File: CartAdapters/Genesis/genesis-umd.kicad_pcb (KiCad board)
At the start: 2 copper layers, 26.7 x 94.6 mm, 6 parts, among them CON101 UMDv2-CONN, CON102 GENESIS-CONN, U101 MCP23008T-E_SS

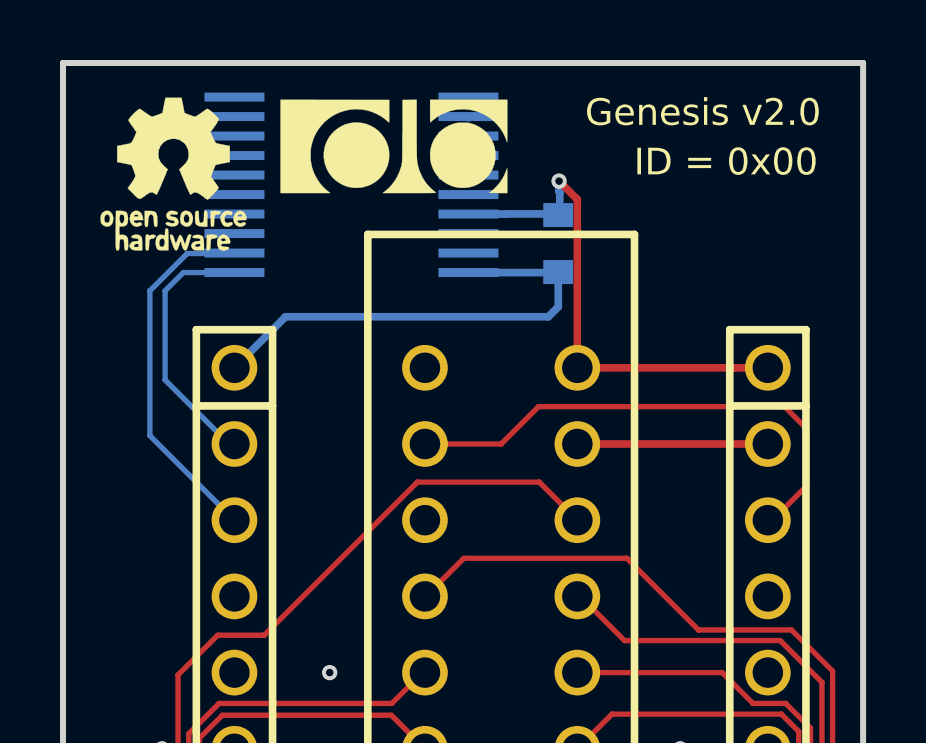
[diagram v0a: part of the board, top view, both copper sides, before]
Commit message: added 0 jumpers for nWR pin selection to support legacy Bitmap Bureau PCBs
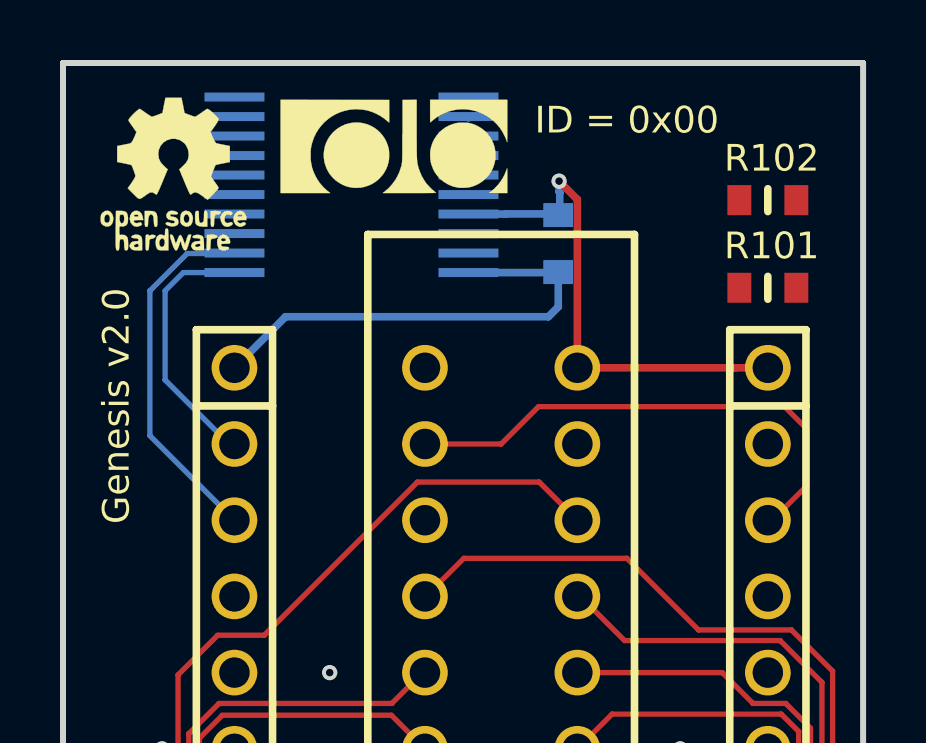
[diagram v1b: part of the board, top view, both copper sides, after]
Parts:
- added R101: 0, db-smt:0603, F.Cu at (153.7, 63.4)
- added R102: 0, db-smt:0603, F.Cu at (153.7, 60.5)
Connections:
- CON102 pad A2: /5V_0 -> Net-(CON102-PadA2)
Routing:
- net /5V_0: track 6.38 -> 0.00 mm
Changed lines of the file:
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@@
     (thickness 1.6)
     (drawings 7)
-    (tracks 500)
+    (tracks 499)
     (zones 0)
-    (modules 6)
-    (nets 58)
+    (modules 8)
+    (nets 59)
   )
   (page A4)
@@
   (net 56 /5V_0)
   (net 57 /5V_1)
+  (net 58 "Net-(CON102-PadA2)")
   (net_class Default "This is the default net class."
     (clearance 0.1778)
@@
     (uvia_dia 0.3)
     (uvia_drill 0.1)
+    (add_net /A0)
     (add_net /A1)
     (add_net /A10)
@@
     (add_net /~VRES~)
     (add_net /~WR~)
+    (add_net "Net-(CON101-Pad25)")
+    (add_net "Net-(CON101-Pad4)")
+    (add_net "Net-(CON101-Pad40)")
+    (add_net "Net-(CON101-Pad5)")
+    (add_net "Net-(CON101-Pad60)")
+    (add_net "Net-(CON101-Pad61)")
+    (add_net "Net-(CON101-Pad65)")
+    (add_net "Net-(CON101-Pad66)")
+    (add_net "Net-(CON102-PadA2)")
+    (add_net "Net-(CON102-PadB1)")
+    (add_net "Net-(CON102-PadB12)")
+    (add_net "Net-(CON102-PadB13)")
+    (add_net "Net-(CON102-PadB14)")
+    (add_net "Net-(CON102-PadB15)")
+    (add_net "Net-(CON102-PadB19)")
+    (add_net "Net-(CON102-PadB21)")
+    (add_net "Net-(CON102-PadB3)")
+    (add_net "Net-(U101-Pad10)")
+    (add_net "Net-(U101-Pad11)")
+    (add_net "Net-(U101-Pad7)")
   )
   (net_class Power ""
@@
     (add_net /5V_1)
     (add_net GND)
+  )
+  (module db-smt:0603 (layer F.Cu)
+    (at 153.67 60.452)
+    (tags 0603)
+    (solder_mask_margin 0.1016)
+    (attr smd)
+    (fp_text reference R102 (at 0.127 -1.397) (layer F.SilkS)
+      (effects (font (size 0.889 0.889) (thickness 0.2032)))
+    )
+    (fp_text value 0 (at 0.508 -2.54) (layer F.Fab) hide
+      (effects (font (size 1 1) (thickness 0.15)))
+    )
+    (fp_line (start 0 -0.381) (end 0 0.381) (layer F.SilkS) (width 0.254))
+    (pad 2 smd rect (at 0.95 0) (size 0.8 1) (layers F.Cu F.Paste F.Mask)
+      (net 10 /~WR~))
+    (pad 1 smd rect (at -0.95 0) (size 0.8 1) (layers F.Cu F.Paste F.Mask)
+      (net 58 "Net-(CON102-PadA2)"))
+    (model Resistors_SMD.3dshapes/R_0603.wrl
+      (at (xyz 0 0 0))
+      (scale (xyz 1 1 1))
+      (rotate (xyz 0 0 0))
+    )
+  )
+  (module db-smt:0603 (layer F.Cu)
+    (at 153.67 63.373)
+    (tags 0603)
+    (solder_mask_margin 0.1016)
+    (attr smd)
+    (fp_text reference R101 (at 0.127 -1.397) (layer F.SilkS)
+      (effects (font (size 0.889 0.889) (thickness 0.2032)))
+    )
+    (fp_text value 0 (at 0.508 -2.54) (layer F.Fab) hide
+      (effects (font (size 1 1) (thickness 0.15)))
+    )
+    (fp_line (start 0 -0.381) (end 0 0.381) (layer F.SilkS) (width 0.254))
+    (pad 2 smd rect (at 0.95 0) (size 0.8 1) (layers F.Cu F.Paste F.Mask)
+      (net 56 /5V_0))
+    (pad 1 smd rect (at -0.95 0) (size 0.8 1) (layers F.Cu F.Paste F.Mask)
+      (net 58 "Net-(CON102-PadA2)"))
+    (model Resistors_SMD.3dshapes/R_0603.wrl
+      (at (xyz 0 0 0))
+      (scale (xyz 1 1 1))
+      (rotate (xyz 0 0 0))
+    )
   )
   (module db-artwork:db-logo_7.5mm (layer F.Cu)
@@
       (net 2 GND))
     (pad A2 thru_hole circle (at 5.08 2.54 180) (size 1.524 1.524) (drill 1.016) (layers *.Cu *.Mask)
-      (net 56 /5V_0))
+      (net 58 "Net-(CON102-PadA2)"))
     (pad A3 thru_hole circle (at 5.08 5.08 180) (size 1.524 1.524) (drill 1.016) (layers *.Cu *.Mask)
       (net 12 /A8))
@@
       (net 2 GND))
   )
-  (gr_text "ID = 0x00" (at 152.273 59.182) (layer F.SilkS)
+  (gr_text "ID = 0x00" (at 148.971 57.785) (layer F.SilkS)
     (effects (font (size 0.889 0.889) (thickness 0.1524)))
   )
-  (gr_text "Genesis v2.0" (at 151.511 57.531) (layer F.SilkS)
+  (gr_text "Genesis v2.0" (at 131.953 67.31 90) (layer F.SilkS)
     (effects (font (size 0.889 0.889) (thickness 0.1524)))
   )
@@
   (segment (start 134.9756 135.763) (end 134.3406 135.128) (width 0.1778) (layer F.Cu) (net 55))
   (segment (start 141.6304 133.3754) (end 139.2428 135.763) (width 0.1778) (layer F.Cu) (net 55))
-  (segment (start 147.32 68.58) (end 153.6954 68.58) (width 0.254) (layer F.Cu) (net 56))
   (segment (start 147.32 142.24) (end 153.67 142.24) (width 0.254) (layer B.Cu) (net 57))
   (zone (net 0) (net_name "") (layers F&B.Cu) (hatch edge 0.508)
@@
     (connect_pads (clearance 0.254))
     (min_thickness 0.1778)
-    (fill yes (arc_segments 16) (thermal_gap 0.254) (thermal_bridge_width 0.254))
+    (fill (arc_segments 16) (thermal_gap 0.254) (thermal_bridge_width 0.254))
     (polygon
       (pts
@@
     (connect_pads (clearance 0.254))
     (min_thickness 0.1778)
-    (fill yes (arc_segments 16) (thermal_gap 0.254) (thermal_bridge_width 0.254))
+    (fill (arc_segments 16) (thermal_gap 0.254) (thermal_bridge_width 0.254))
     (polygon
       (pts
